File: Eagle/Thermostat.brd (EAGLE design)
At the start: 67.1 x 49.3 mm, 57 parts, among them J2 USB-MINIB-5PIN, K1 AQY282EHA, K2 AQY282EHA, K3 AQY282EHA, K4 AQY282EHA, K5 AQY282EHA, Q1 MOSFET-PCHANNELSMD

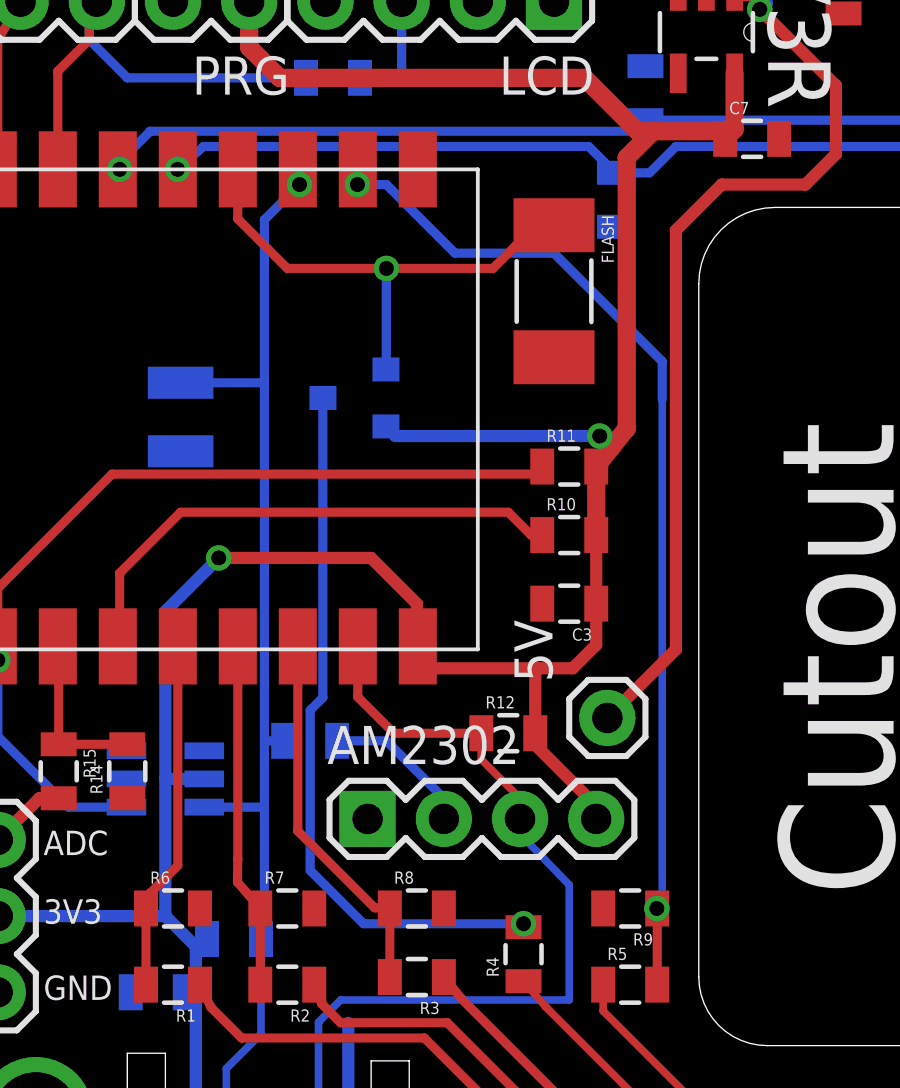
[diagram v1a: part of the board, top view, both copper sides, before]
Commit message: Added R20 before PNP
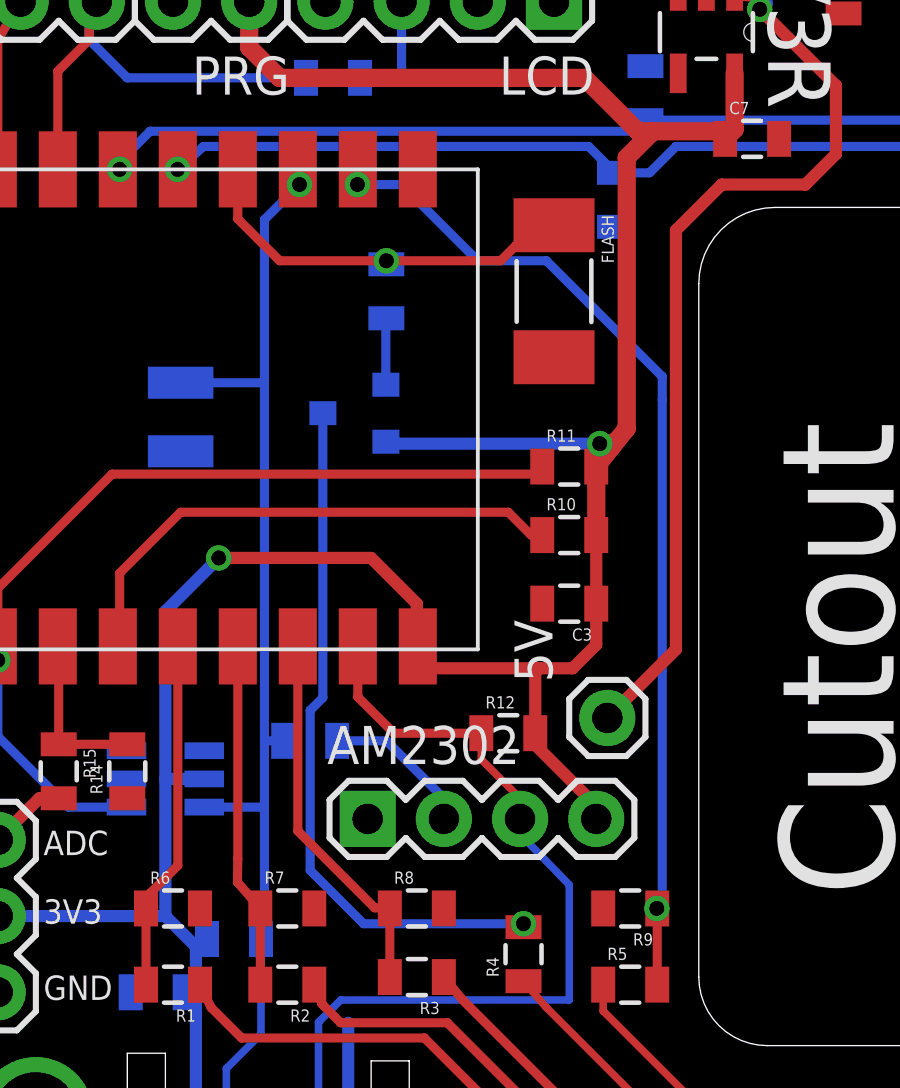
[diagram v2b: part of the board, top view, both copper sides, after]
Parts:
- added R20: 1K, SparkFun-Passives:0805
- moved Q1 0.51 mm to (13.7, 26.4)
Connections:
- new net N$1: Q1.1, R20.1
- net HUMID: now also R20.2; no longer Q1.1
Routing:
- net HUMID: track 16.7 -> 13.3 mm
- net N$1: track 0.00 -> 2.21 mm
- net N$9: track 24.9 -> 24.4 mm
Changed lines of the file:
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@@
 <attribute name="OC_FARNELL" value="unknown" x="40.894" y="20.32" size="0.8128" layer="27" ratio="16" rot="R270" display="off"/>
 </element>
-<element name="Q1" library="SparkFun-DiscreteSemi" package="SOT23-3" value="MOSFET-PCHANNELSMD" x="13.716" y="26.924" rot="MR270"/>
+<element name="Q1" library="SparkFun-DiscreteSemi" package="SOT23-3" value="MOSFET-PCHANNELSMD" x="13.716" y="26.416" rot="MR270"/>
 <element name="R12" library="SparkFun-Resistors" package="0805" value="4K7" x="18.796" y="15.748"/>
 <element name="R13" library="SparkFun-Resistors" package="0805" value="4K7" x="9.652" y="8.89" rot="MR0"/>
@@
 <element name="C9" library="SparkFun-Capacitors" package="0805" value="0.1uF" x="7.112" y="7.112" rot="MR0"/>
 <element name="R19" library="SparkFun-Resistors" package="0805" value="10K" x="10.16" y="43.434" rot="MR90"/>
+<element name="R20" library="SparkFun-Passives" package="0805" value="1K" x="14.732" y="30.48" rot="MR90"/>
 </elements>
 <signals>
@@
 <wire x1="13.78" y1="33.846" x2="13.7668" y2="34.036" width="0.3048" layer="1"/>
 <via x="13.7668" y="34.036" extent="1-16" drill="0.5" shape="square"/>
-<wire x1="13.7668" y1="34.036" x2="14.732" y2="34.036" width="0.3048" layer="16"/>
-<wire x1="14.732" y1="34.036" x2="17.018" y2="31.75" width="0.3048" layer="16"/>
-<wire x1="17.018" y1="31.75" x2="20.32" y2="31.75" width="0.3048" layer="16"/>
-<wire x1="20.32" y1="31.75" x2="23.9268" y2="28.1432" width="0.3048" layer="16"/>
-<wire x1="23.9268" y1="28.1432" x2="23.9268" y2="26.8732" width="0.3048" layer="16"/>
+<wire x1="13.7668" y1="34.036" x2="15.24" y2="34.036" width="0.3048" layer="16"/>
+<wire x1="15.24" y1="34.036" x2="17.78" y2="31.496" width="0.3048" layer="16"/>
+<wire x1="17.78" y1="31.496" x2="20.066" y2="31.496" width="0.3048" layer="16"/>
+<wire x1="20.066" y1="31.496" x2="23.9268" y2="27.6352" width="0.3048" layer="16"/>
+<wire x1="23.9268" y1="27.6352" x2="23.9268" y2="26.8732" width="0.3048" layer="16"/>
 <wire x1="13.78" y1="33.846" x2="13.78" y2="33.7952" width="0.3048" layer="1"/>
 <wire x1="13.78" y1="33.7952" x2="13.7668" y2="33.782" width="0.3048" layer="1"/>
 <wire x1="23.749" y1="9.906" x2="23.76" y2="9.906" width="0.6096" layer="1"/>
 <wire x1="23.749" y1="9.906" x2="23.9268" y2="10.0838" width="0.254" layer="16"/>
-<wire x1="23.9268" y1="10.0838" x2="23.9268" y2="26.8732" width="0.254" layer="16"/>
+<wire x1="23.9268" y1="10.0838" x2="23.9268" y2="26.8732" width="0.3048" layer="16"/>
 </signal>
 <signal name="N$25">
@@
 <contactref element="SHT21" pad="5"/>
 <wire x1="9.422" y1="2.286" x2="8.382" y2="2.286" width="0.4064" layer="16"/>
-<via x="21.844" y="25.654" extent="1-16" drill="0.5" shape="square"/>
-<wire x1="21.844" y1="25.654" x2="22.38121875" y2="25.654" width="0.3048" layer="1"/>
+<via x="21.844" y="25.4" extent="1-16" drill="0.5" shape="square"/>
+<wire x1="21.844" y1="25.4" x2="22.38121875" y2="25.654" width="0.3048" layer="1"/>
 <wire x1="22.38121875" y1="25.654" x2="22.244096875" y2="25.283121875" width="0.3048" layer="1"/>
-<wire x1="14.716" y1="25.974" x2="15.036" y2="25.654" width="0.4064" layer="16"/>
-<wire x1="15.036" y1="25.654" x2="21.844" y2="25.654" width="0.4064" layer="16"/>
+<wire x1="14.716" y1="25.466" x2="15.036" y2="25.4" width="0.4064" layer="16"/>
+<wire x1="15.036" y1="25.4" x2="21.844" y2="25.4" width="0.4064" layer="16"/>
 <contactref element="C9" pad="1"/>
 <wire x1="8.012" y1="7.112" x2="8.382" y2="7.112" width="0.254" layer="16"/>
@@
 <contactref element="R4" pad="2"/>
 <contactref element="Q1" pad="3"/>
-<wire x1="12.616" y1="26.924" x2="12.616" y2="16.934" width="0.3048" layer="16"/>
+<wire x1="12.616" y1="26.416" x2="12.616" y2="16.934" width="0.3048" layer="16"/>
 <wire x1="12.616" y1="16.934" x2="12.192" y2="16.51" width="0.3048" layer="16"/>
 <wire x1="12.192" y1="16.51" x2="12.192" y2="11.176" width="0.3048" layer="16"/>
@@
 </signal>
 <signal name="HUMID">
-<contactref element="Q1" pad="1"/>
 <contactref element="U$1" pad="GPIO0"/>
 <contactref element="FLASH" pad="1"/>
-<via x="14.732" y="31.242" extent="1-16" drill="0.5" shape="square"/>
+<via x="14.732" y="31.496" extent="1-16" drill="0.5" shape="square"/>
 <wire x1="9.78" y1="34.542" x2="9.779" y2="34.541" width="0.3048" layer="1"/>
 <wire x1="9.779" y1="34.541" x2="9.779" y2="32.893" width="0.3048" layer="1"/>
-<wire x1="9.779" y1="32.893" x2="11.43" y2="31.242" width="0.3048" layer="1"/>
-<wire x1="11.43" y1="31.242" x2="14.732" y2="31.242" width="0.3048" layer="1"/>
+<wire x1="9.779" y1="32.893" x2="11.176" y2="31.496" width="0.3048" layer="1"/>
+<wire x1="11.176" y1="31.496" x2="14.732" y2="31.496" width="0.3048" layer="1"/>
 <wire x1="20.32" y1="32.68" x2="19.05" y2="32.004" width="0.3048" layer="1"/>
-<wire x1="19.05" y1="32.004" x2="18.288" y2="31.242" width="0.3048" layer="1"/>
-<wire x1="18.288" y1="31.242" x2="14.732" y2="31.242" width="0.3048" layer="1"/>
-<wire x1="14.716" y1="27.874" x2="14.716" y2="27.924" width="0.3048" layer="16"/>
-<wire x1="14.716" y1="27.924" x2="14.732" y2="28.448" width="0.3048" layer="16"/>
-<wire x1="14.732" y1="28.448" x2="14.732" y2="31.242" width="0.3048" layer="16"/>
+<wire x1="19.05" y1="32.004" x2="18.542" y2="31.496" width="0.3048" layer="1"/>
+<wire x1="18.542" y1="31.496" x2="14.732" y2="31.496" width="0.3048" layer="1"/>
+<contactref element="R20" pad="2"/>
+<wire x1="14.732" y1="31.38" x2="14.732" y2="31.496" width="0.3048" layer="16"/>
 </signal>
 <signal name="RXD2">
@@
 <contactref element="SHT21" pad="3"/>
 </signal>
+<signal name="N$1">
+<contactref element="Q1" pad="1"/>
+<contactref element="R20" pad="1"/>
+<wire x1="14.732" y1="29.58" x2="14.716" y2="29.326" width="0.3048" layer="16"/>
+<wire x1="14.716" y1="29.326" x2="14.716" y2="27.366" width="0.3048" layer="16"/>
+</signal>
 </signals>

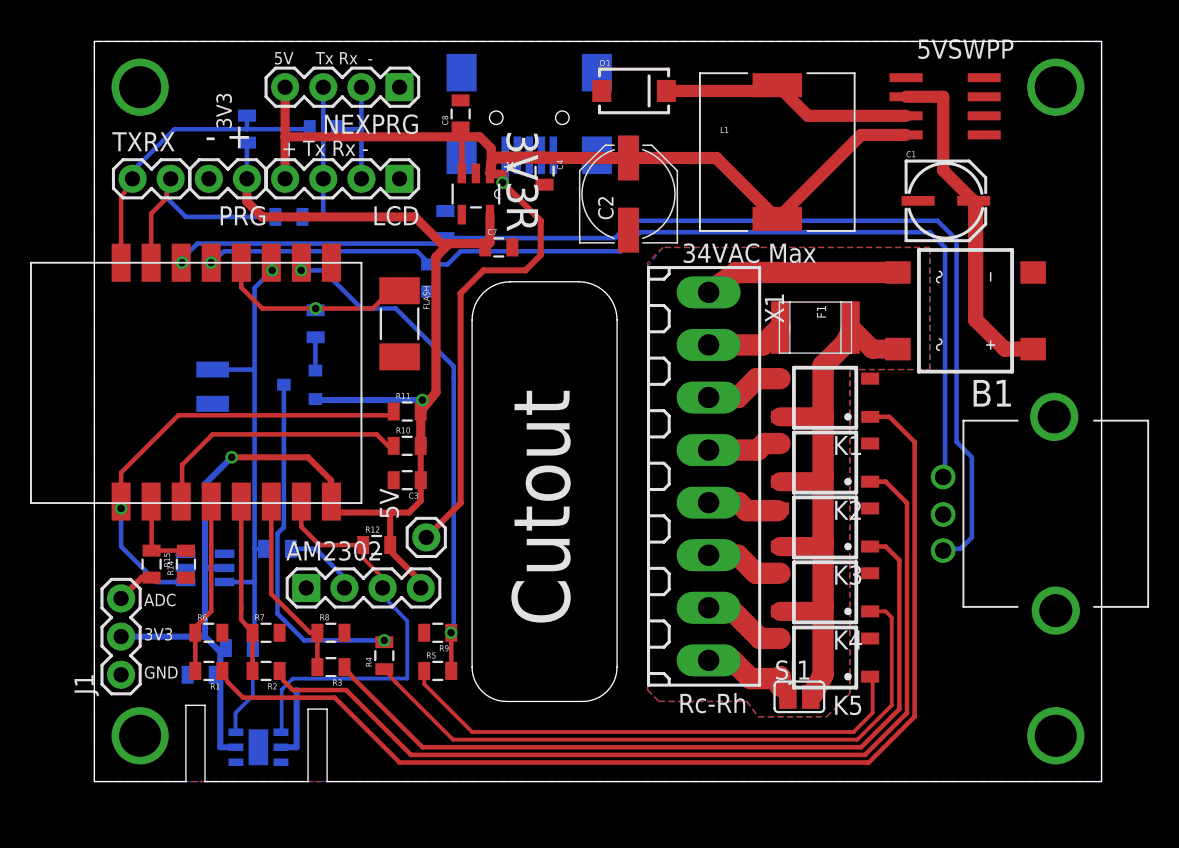
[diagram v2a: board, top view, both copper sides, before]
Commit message: Moved USB to top
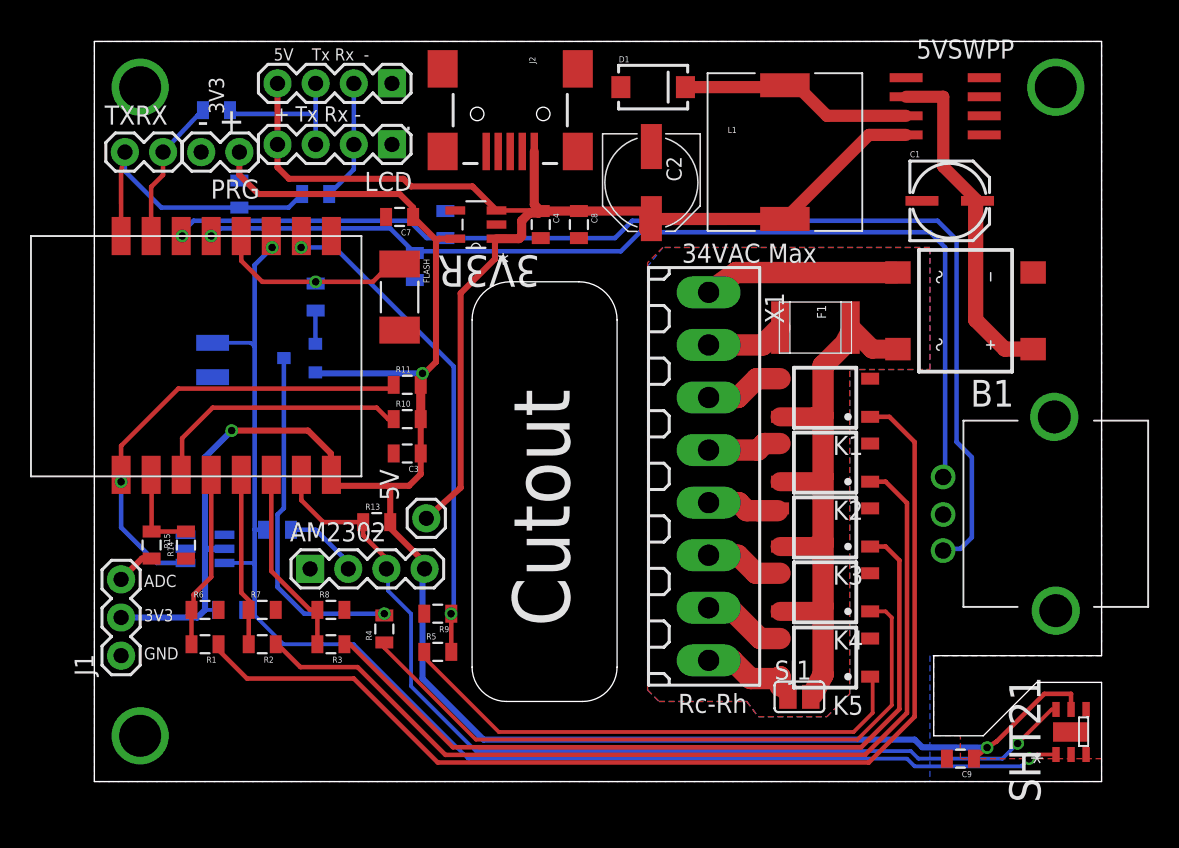
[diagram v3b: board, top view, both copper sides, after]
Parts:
- removed NEXPRG: (no value), SparkFun-Connectors:1X04
- added .: (no value), SparkFun-Connectors:1X04
- 3V3R: value MCP1801T-3302I/OT -> MCP1755T-3302E/OT
- R20: value 1K -> 4K7
- moved SHT21 54.1 mm to (65.0, 3.30), flipped to the top, turned to 90 degrees
- moved C9 50.9 mm to (57.7, 1.52), flipped to the top, turned to 180 degrees
- moved R13 12.4 mm to (18.8, 17.3), flipped to the top
- moved C8 10.8 mm to (32.3, 37.1), turned to 270 degrees
- moved R12 10.6 mm to (9.14, 11.4), flipped to the bottom
- moved R16 8.59 mm to (8.13, 44.7)
- moved C7 6.91 mm to (20.3, 37.6), turned to 180 degrees
- moved R17 4.35 mm to (14.7, 39.1)
- moved R19 4.35 mm to (9.65, 39.1), turned to 270 degrees
- moved C4 3.57 mm to (29.7, 37.1)
- moved LCD 2.34 mm to (19.8, 42.4)
- moved 3V3R 2.03 mm to (25.4, 37.1), turned to 180 degrees
- moved PRG 1.85 mm to (9.65, 41.9)
- moved TXRX 1.85 mm to (2.03, 41.9)
- moved R1 1.80 mm to (7.37, 9.14)
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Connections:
- net 5V: now also ..4; no longer NEXPRG.4
- net GND: now also ..1; no longer NEXPRG.1
- net RXD2: now also ..3; no longer NEXPRG.3
- net SCL: now also AM2302.3, U$1.GPIO13; no longer 10F.6, R18.1, U$1.GPIO2, U$5.>NAME
- net SDA: now also 10F.6, R18.1, U$1.GPIO2, U$5.>NAME; no longer AM2302.3, U$1.GPIO13
- net TXD2: now also ..2; no longer NEXPRG.2
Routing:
- net SDA: track 27.9 -> 91.1 mm, vias 0 -> 2
- net 3V3: track 100.9 -> 143.1 mm, vias 2 -> 3
- net SCL: track 39.2 -> 64.9 mm
- net 5V: track 91.7 -> 83.3 mm, vias 1 -> 0
- net RXD: track 15.3 -> 9.77 mm
- net GND: track 4.85 -> 0.00 mm
- net N$4: track 72.0 -> 73.1 mm
- net N$2: track 17.0 -> 15.9 mm
- net N$7: track 62.4 -> 63.4 mm
- net N$14: track 44.2 -> 45.1 mm
- net HEAT: track 34.3 -> 33.5 mm
- net N$10: track 52.5 -> 53.1 mm
- net ADC: track 5.58 -> 6.09 mm
- net REST: track 30.4 -> 30.9 mm
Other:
- outline, holes or cut-outs redrawn

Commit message: r1 - better, but not perfect
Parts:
- moved SHT21 63.2 mm to (1.78, 3.00), turned to 270 degrees
- moved C9 38.6 mm to (19.1, 1.27), turned to 0 degrees
- moved 10F 2.29 mm to (7.37, 17.8)
- moved J1 1.52 mm to (1.78, 9.91)
- moved R12 1.37 mm to (8.64, 12.7)
- moved R15 0.25 mm to (4.06, 15.7)
- moved R14 0.25 mm to (6.35, 15.7)
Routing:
- net SDA: track 91.1 -> 56.2 mm
- net SCL: track 64.9 -> 39.9 mm
- net 3V3: track 143.1 -> 118.2 mm
- net REST: track 30.9 -> 28.7 mm
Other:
- outline, holes or cut-outs redrawn
